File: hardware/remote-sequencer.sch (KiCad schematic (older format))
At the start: 24 parts, among them J1 PWR_IN, J2 RF_SENSE_BOARD, J3 RELAY_LED_OUT, J4 RELAY_OUT, J5 RF_SENSE_DISABLE, J6 DTMF_MODULE, J7 ON, J8 OFF, U1 LM7805_TO220

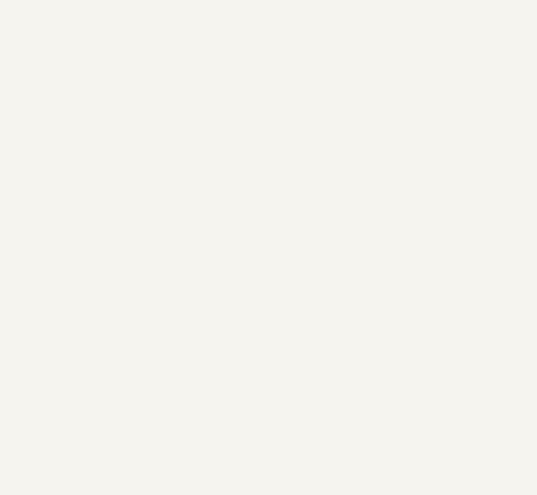
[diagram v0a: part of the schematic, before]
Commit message: adds relay board schematic and pcb
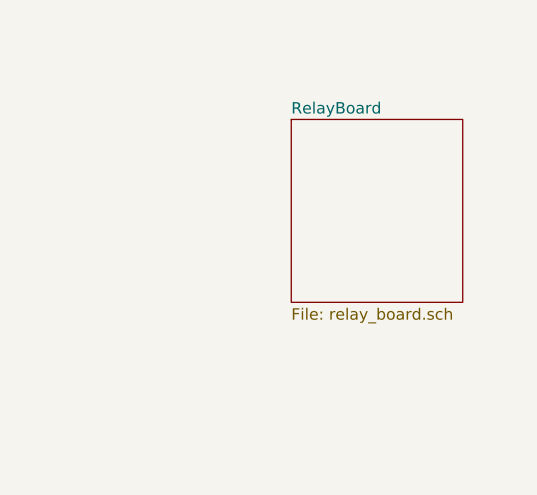
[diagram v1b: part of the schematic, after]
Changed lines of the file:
@@
 $Descr A4 11693 8268
 encoding utf-8
-Sheet 1 1
+Sheet 1 2
 Title "Main board"
 Date "2018-12-19"
@@
 	1600 3800 1950 3800
 Connection ~ 1950 3800
+$Sheet
+S 8850 2300 750  800
+U 5C1E9383
+F0 "RelayBoard" 50
+F1 "relay_board.sch" 50
+$EndSheet
 $EndSCHEMATC

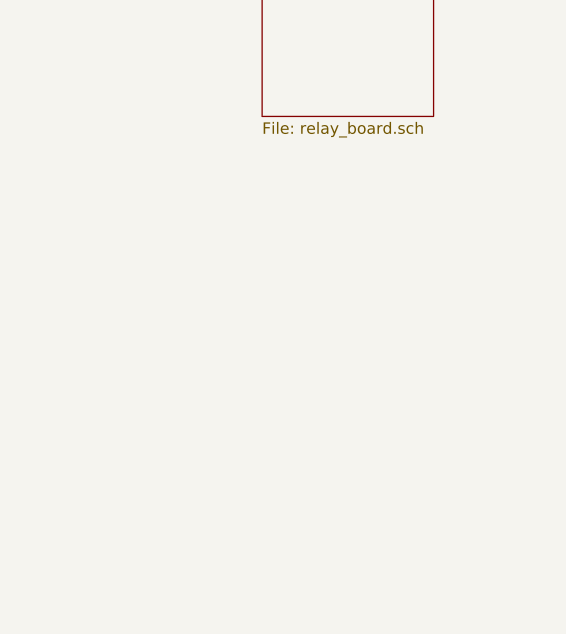
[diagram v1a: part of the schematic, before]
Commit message: adds rf sense board schematic and pcb
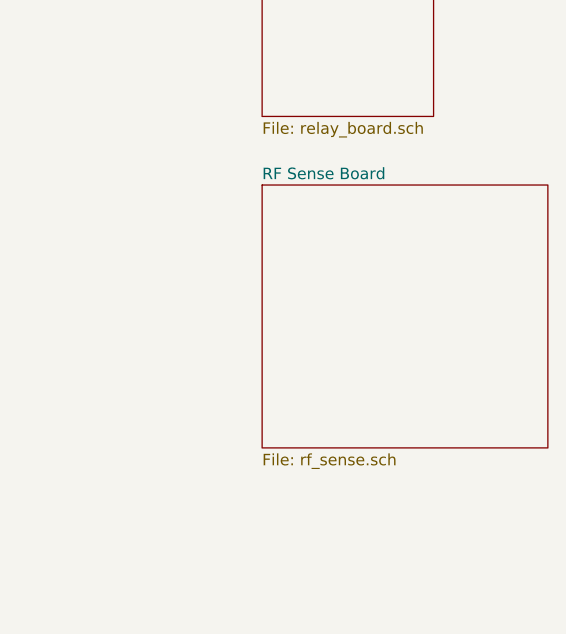
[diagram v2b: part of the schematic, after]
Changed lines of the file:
@@
 $Descr A4 11693 8268
 encoding utf-8
-Sheet 1 2
+Sheet 1 3
 Title "Main board"
 Date "2018-12-19"
@@
 F1 "relay_board.sch" 50
 $EndSheet
+$Sheet
+S 8850 3400 1250 1150
+U 5C24E8B1
+F0 "RF Sense Board" 50
+F1 "rf_sense.sch" 50
+$EndSheet
 $EndSCHEMATC
